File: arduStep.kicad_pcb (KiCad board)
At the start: 2 copper layers, 29 x 50 mm, 11 parts, among them J1 stepper, J2 jst battery, U1 ULN2003A

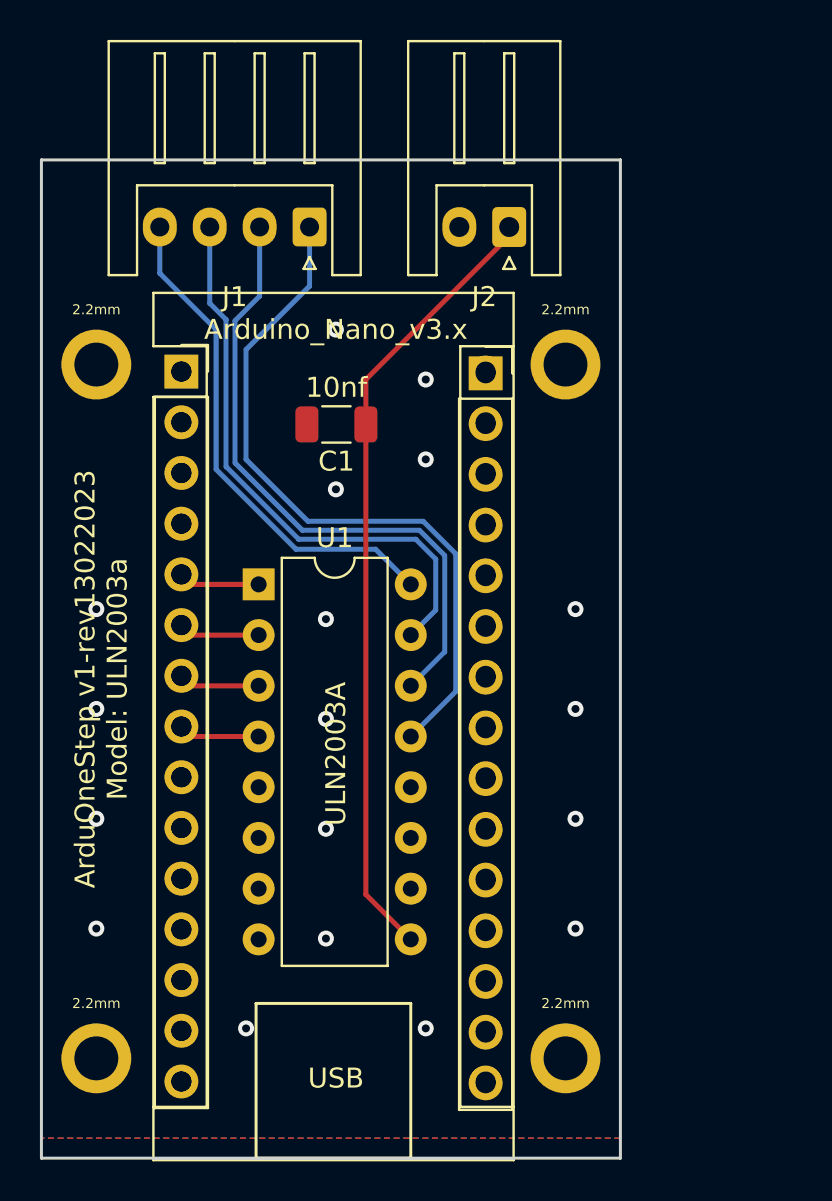
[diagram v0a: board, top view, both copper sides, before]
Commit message: add gerber files, list of component and edit README
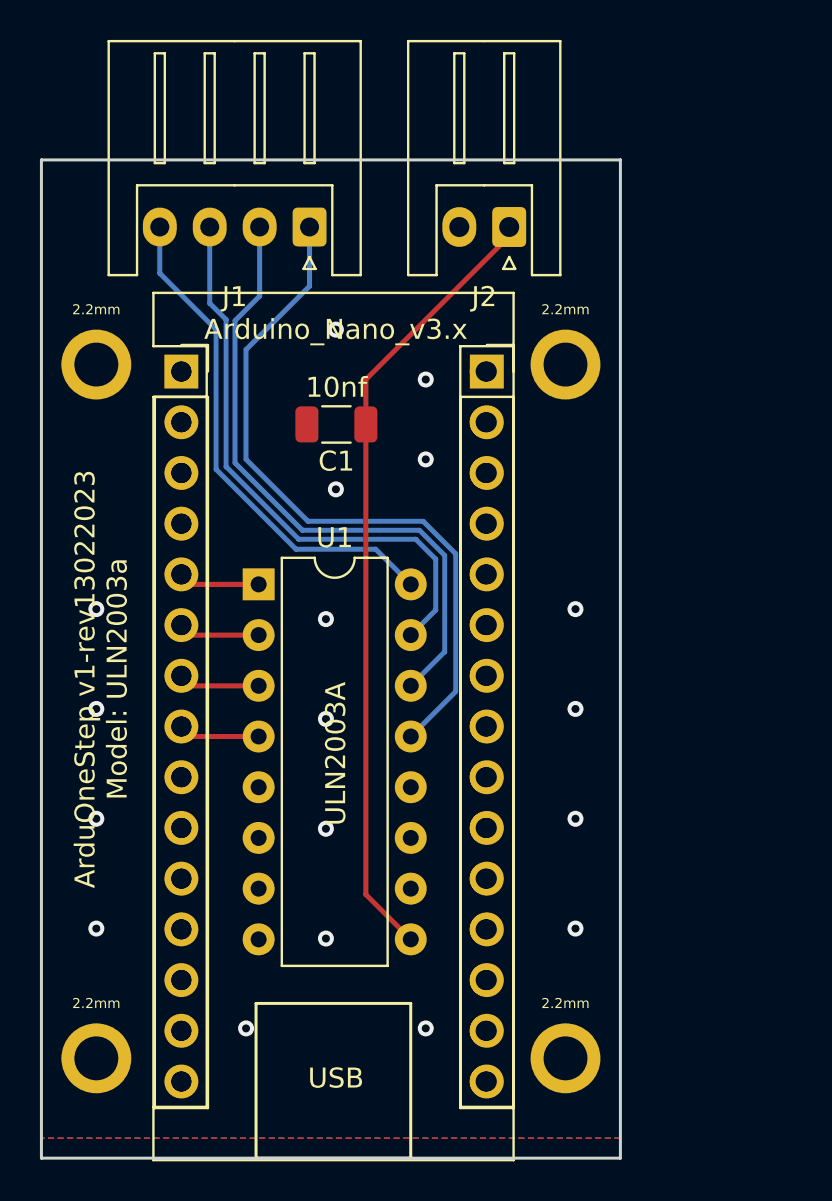
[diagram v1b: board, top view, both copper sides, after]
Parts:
- moved REF** 0.11 mm to (164.1, 67.6)
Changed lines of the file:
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@@
       (outputformat 1)
       (mirror false)
-      (drillshape 1)
+      (drillshape 0)
       (scaleselection 1)
       (outputdirectory "")
@@
     (tags "Through hole socket strip THT 1x15 2.54mm single row")
     (attr through_hole)
-    (fp_text reference "REF**" (at 0 -2.77) (layer "F.SilkS") hide
+    (fp_text reference "REF**" (at 0 -2.77) (layer "Dwgs.User") hide
       (effects (font (size 1 1) (thickness 0.15)))
     )
@@
     (property "Sheetfile" "arduStep.kicad_sch")
     (property "Sheetname" "")
-    (attr through_hole)
+    (attr through_hole board_only exclude_from_pos_files exclude_from_bom)
     (fp_text reference "A1" (at 4.74 -0.1) (layer "F.SilkS") hide
       (effects (font (size 1 1) (thickness 0.15)))
@@
   )
   (footprint "Connector_PinSocket_2.54mm:PinSocket_1x15_P2.54mm_Vertical" (layer "F.Cu")
-    (at 164 67.69)
+    (at 164.06 67.6)
     (descr "Through hole straight socket strip, 1x15, 2.54mm pitch, single row (from Kicad 4.0.7), script generated")
     (tags "Through hole socket strip THT 1x15 2.54mm single row")
     (attr through_hole)
-    (fp_text reference "REF**" (at 0 -2.77) (layer "F.SilkS") hide
+    (fp_text reference "REF**" (at 0 -2.77) (layer "Dwgs.User") hide
       (effects (font (size 1 1) (thickness 0.15)))
     )
@@
     (fp_line (start 0 1.2) (end 0.625 2.2) (layer "F.Fab") (width 0.1))
     (fp_line (start -1.25 -2.3) (end -1.25 2.2) (layer "F.Fab") (width 0.1))
-    (pad "1" thru_hole roundrect (at 0 0 180) (size 1.7 2) (drill 1) (layers *.Cu *.Mask) (roundrect_rratio 0.147059)
+    (pad "1" thru_hole roundrect (at 0 0 180) (size 1.7 2) (drill 1) (layers *.Cu *.Mask) (roundrect_rratio 0.1470588235)
       (net 33 "5V") (pinfunction "Pin_1") (pintype "passive"))
     (pad "2" thru_hole oval (at 2.5 0 180) (size 1.7 2) (drill 1) (layers *.Cu *.Mask)
@@
     (fp_line (start 1.6 0.8) (end -1.6 0.8) (layer "F.Fab") (width 0.1))
     (fp_line (start 1.6 -0.8) (end 1.6 0.8) (layer "F.Fab") (width 0.1))
-    (pad "1" smd roundrect (at -1.475 0 180) (size 1.15 1.8) (layers "F.Cu" "F.Paste" "F.Mask") (roundrect_rratio 0.217391)
+    (pad "1" smd roundrect (at -1.475 0 180) (size 1.15 1.8) (layers "F.Cu" "F.Paste" "F.Mask") (roundrect_rratio 0.2173913043)
       (net 33 "5V") (pintype "passive"))
-    (pad "2" smd roundrect (at 1.475 0 180) (size 1.15 1.8) (layers "F.Cu" "F.Paste" "F.Mask") (roundrect_rratio 0.217391)
+    (pad "2" smd roundrect (at 1.475 0 180) (size 1.15 1.8) (layers "F.Cu" "F.Paste" "F.Mask") (roundrect_rratio 0.2173913043)
       (net 27 "GND") (pintype "passive"))
     (model "${KICAD6_3DMODEL_DIR}/Capacitor_SMD.3dshapes/C_1206_3216Metric.wrl"
@@
     (fp_line (start 3.75 9.2) (end -2.45 9.2) (layer "F.Fab") (width 0.1))
     (fp_line (start 3.75 9.2) (end 9.95 9.2) (layer "F.Fab") (width 0.1))
-    (pad "1" thru_hole roundrect (at 0 0 180) (size 1.7 1.95) (drill 0.95) (layers *.Cu *.Mask) (roundrect_rratio 0.147059)
+    (pad "1" thru_hole roundrect (at 0 0 180) (size 1.7 1.95) (drill 0.95) (layers *.Cu *.Mask) (roundrect_rratio 0.1470588235)
       (net 29 "Net-(J1-Pad1)") (pinfunction "Pin_1") (pintype "passive"))
     (pad "2" thru_hole oval (at 2.5 0 180) (size 1.7 1.95) (drill 0.95) (layers *.Cu *.Mask)

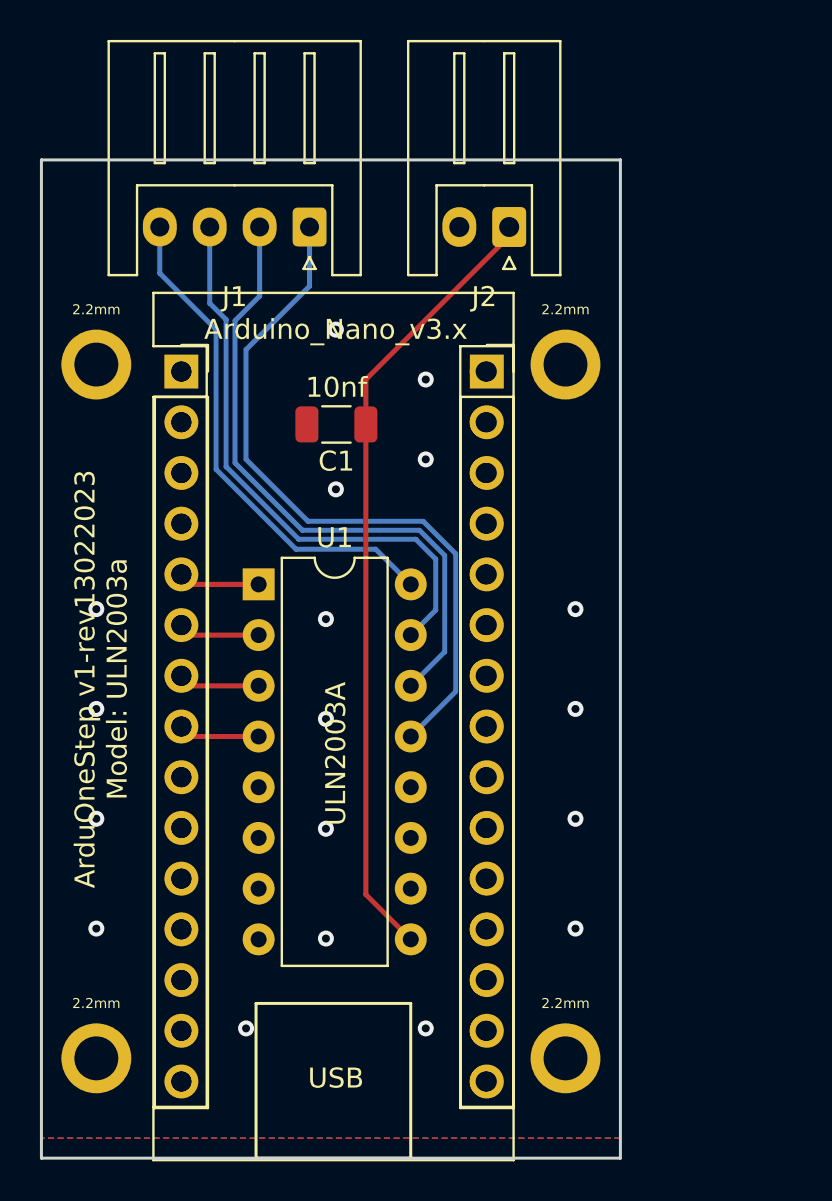
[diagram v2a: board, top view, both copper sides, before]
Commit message: modificación fisica del conector de carga
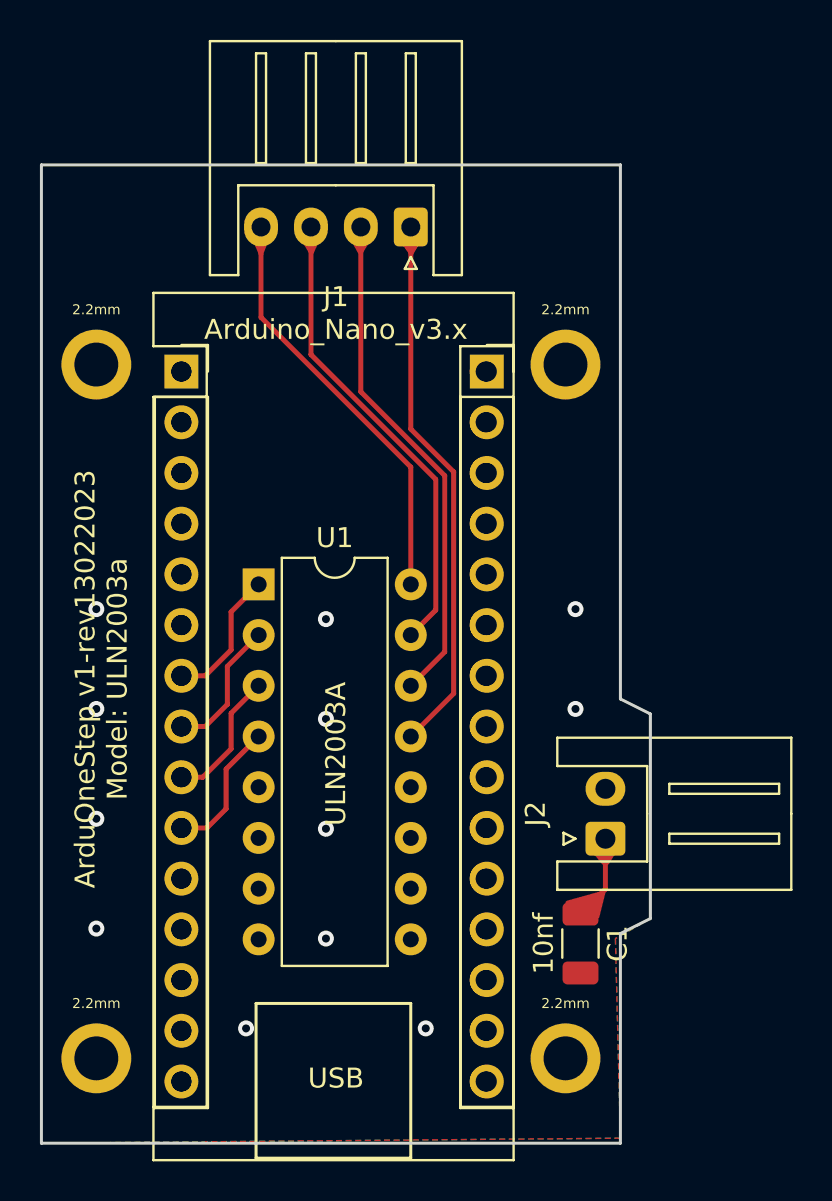
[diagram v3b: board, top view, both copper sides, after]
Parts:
- moved J2 31.0 mm to (170.0, 91.0), turned to 90 degrees
- moved C1 28.7 mm to (168.8, 96.2), turned to -90 degrees
- moved J1 5.07 mm to (160.2, 60.4)
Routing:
- net 5V: track 39.6 -> 4.29 mm
- net Net-(J1-Pad1): track 35.5 -> 27.3 mm
- net /in4: track 0.00 -> 6.93 mm
- net /in3: track 0.00 -> 6.81 mm
- net Net-(J1-Pad2): track 32.0 -> 25.4 mm
- net Net-(J1-Pad3): track 29.1 -> 23.5 mm
- net Net-(J1-Pad4): track 25.4 -> 21.0 mm
- net unconnected-(A1-Pad6): track 4.08 -> 0.00 mm
- net /in1: track 4.08 -> 7.59 mm
- net /in2: track 4.08 -> 7.59 mm
- net unconnected-(A1-Pad5): track 4.08 -> 0.71 mm
- net GND: vias 18 -> 12
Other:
- board size 29 x 50 mm -> 30.5 x 49 mm

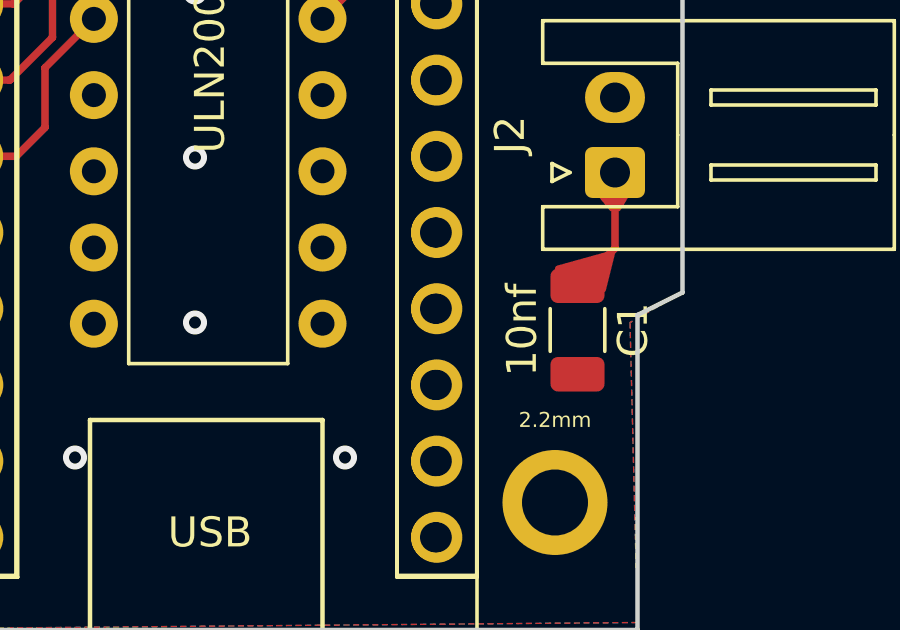
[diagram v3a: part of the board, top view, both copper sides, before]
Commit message: fix route 5v
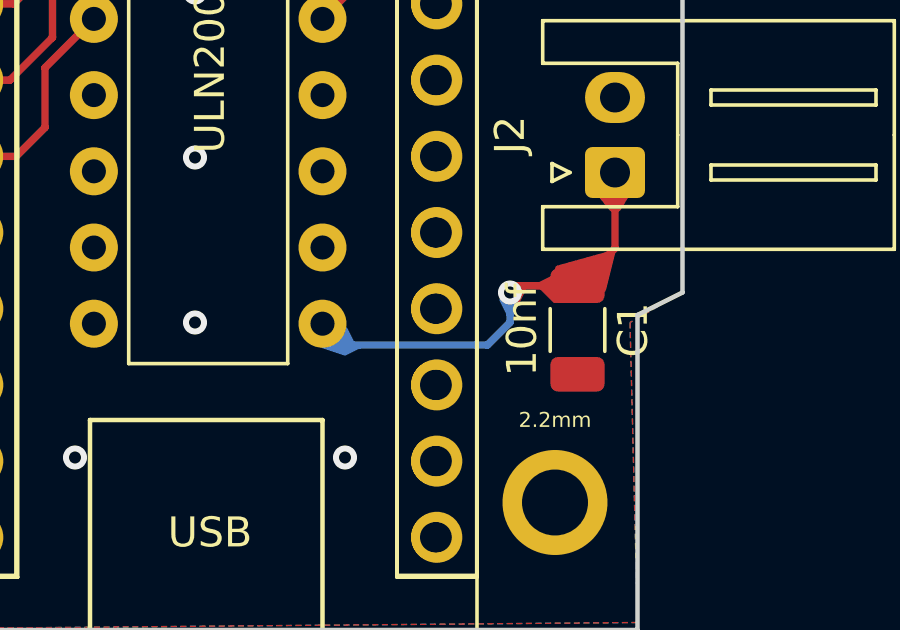
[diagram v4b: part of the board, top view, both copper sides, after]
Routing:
- net 5V: track 4.29 -> 14.5 mm, vias 0 -> 1
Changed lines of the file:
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@@
+  (gr_poly
+    (pts
+      (xy 168 95.25)
+      (xy 167.5 94.75)
+      (xy 168 94.5)
+    ) (layer "F.Cu") (width 0.2) (fill solid))
   (gr_poly
     (pts
@@
   (gr_poly
     (pts
+      (xy 166.75 95.25)
+      (xy 166.5 94.75)
+      (xy 167 94.75)
+    ) (layer "F.Cu") (width 0.2) (fill solid))
+  (gr_poly
+    (pts
       (xy 157.725 61.675)
       (xy 157.45 61.175)
@@
       (xy 170.4 91.7)
     ) (layer "F.Cu") (width 0.2) (fill solid))
+  (gr_poly
+    (pts
+      (xy 166.5 95.75)
+      (xy 166.25 95.25)
+      (xy 166.75 95.25)
+    ) (layer "B.Cu") (width 0.2) (fill solid))
+  (gr_poly
+    (pts
+      (xy 161.25 96.75)
+      (xy 161.5 96.75)
+      (xy 161 97)
+      (xy 160.25 96.75)
+      (xy 161 96.25)
+    ) (layer "B.Cu") (width 0.2) (fill solid))
   (gr_rect (start 152.5 99.25) (end 160.25 107) (layer "F.SilkS") (width 0.15) (fill none))
   (gr_line (start 170.75 106.25) (end 141.75 106.25) (layer "Edge.Cuts") (width 0.15))
@@
   (segment (start 170 91) (end 170 93.525) (width 0.25) (layer "F.Cu") (net 33))
   (segment (start 170 93.525) (end 168.75 94.775) (width 0.25) (layer "F.Cu") (net 33))
+  (segment (start 168.75 94.775) (end 166.725 94.775) (width 0.25) (layer "F.Cu") (net 33))
+  (segment (start 166.725 94.775) (end 166.5 95) (width 0.25) (layer "F.Cu") (net 33))
+  (via (at 166.5 95) (size 0.8) (drill 0.4) (layers "F.Cu" "B.Cu") (net 33))
+  (segment (start 166.5 96) (end 166.5 95) (width 0.25) (layer "B.Cu") (net 33))
+  (segment (start 160.25 96.04) (end 160.96 96.75) (width 0.25) (layer "B.Cu") (net 33))
+  (segment (start 160.96 96.75) (end 165.75 96.75) (width 0.25) (layer "B.Cu") (net 33))
+  (segment (start 165.75 96.75) (end 166.5 96) (width 0.25) (layer "B.Cu") (net 33))
   (segment (start 149.26 78.26) (end 148.76 77.76) (width 0.25) (layer "F.Cu") (net 41))
   (zone (net 27) (net_name "GND") (layers F&B.Cu) (hatch edge 0.508)
